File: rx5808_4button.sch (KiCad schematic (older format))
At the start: 53 parts, among them IC1 ATMEGA328-A, P1 CONN_01X02, P2 CONN_01X05, P3 CONN_02X03, P4 BNC, P5 BNC, P6 BNC, P7 CONN_01X02, SW1 SWITCH_INV, SW2 SW_PUSH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

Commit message: schaltplan weiter und mehr Footprints erstellt
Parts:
- removed D4, D5, D6, D7: weiß, LEDs:LED-0603, symbol LED
- removed R13, R14, R15, R16: 470, Resistors_SMD:R_0603, symbol R
- C5: value 22µ -> 10µ
- SW1: footprint (none) -> Apem:2543xN
- U2: footprint (none) -> Foxtech:RX5808
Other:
- note added: "Taster"
- note removed: "Taster mit Beleuchtung"
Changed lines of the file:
@@
 F 0 "U2" H 8400 2350 60  0000 C CNN
 F 1 "RX5808" H 8000 2350 60  0000 C CNN
-F 2 "" H 6750 2250 60  0001 C CNN
+F 2 "Foxtech:RX5808" H 6750 2250 60  0001 C CNN
 F 3 "" H 6750 2250 60  0000 C CNN
 	1    8200 3050
@@
 F 0 "SW1" H 8000 4450 50  0000 C CNN
 F 1 "SWITCH_INV" H 8050 4150 50  0000 C CNN
-F 2 "" H 8200 4300 60  0001 C CNN
+F 2 "Apem:2543xN" H 8200 4300 60  0001 C CNN
 F 3 "" H 8200 4300 60  0000 C CNN
 	1    8200 4300
@@
 P 3000 2900
 F 0 "C5" H 3050 3000 50  0000 L CNN
-F 1 "22µ" H 3050 2800 50  0000 L CNN
+F 1 "10µ" H 3050 2800 50  0000 L CNN
 F 2 "Capacitors_SMD:C_1206" H 3038 2750 30  0000 C CNN
 F 3 "" H 3000 2900 60  0000 C CNN
@@
 $EndComp
 $Comp
-L LED D4
-U 1 1 54EED267
-P 7600 6100
-F 0 "D4" H 7600 6200 50  0000 C CNN
-F 1 "weiß" H 7600 6000 50  0000 C CNN
-F 2 "LEDs:LED-0603" H 7600 6100 60  0001 C CNN
-F 3 "" H 7600 6100 60  0000 C CNN
-	1    7600 6100
-	0    1    1    0
-$EndComp
-$Comp
-L R R13
-U 1 1 54EED2CC
-P 7600 5650
-F 0 "R13" V 7680 5650 50  0000 C CNN
-F 1 "470" V 7607 5651 50  0000 C CNN
-F 2 "Resistors_SMD:R_0603" V 7530 5650 30  0001 C CNN
-F 3 "" H 7600 5650 30  0000 C CNN
-	1    7600 5650
-	1    0    0    -1
-$EndComp
-$Comp
-L GND #PWR050
-U 1 1 54EED36A
-P 7600 6300
-F 0 "#PWR050" H 7600 6050 60  0001 C CNN
-F 1 "GND" H 7600 6150 60  0000 C CNN
-F 2 "" H 7600 6300 60  0000 C CNN
-F 3 "" H 7600 6300 60  0000 C CNN
-	1    7600 6300
-	1    0    0    -1
-$EndComp
-$Comp
 L GND #PWR051
 U 1 1 54EED3A0
@@
 $EndComp
 $Comp
-L LED D5
-U 1 1 54EED5DC
-P 8200 6100
-F 0 "D5" H 8200 6200 50  0000 C CNN
-F 1 "weiß" H 8200 6000 50  0000 C CNN
-F 2 "LEDs:LED-0603" H 8200 6100 60  0001 C CNN
-F 3 "" H 8200 6100 60  0000 C CNN
-	1    8200 6100
-	0    1    1    0
-$EndComp
-$Comp
-L R R14
-U 1 1 54EED5E2
-P 8200 5650
-F 0 "R14" V 8280 5650 50  0000 C CNN
-F 1 "470" V 8207 5651 50  0000 C CNN
-F 2 "Resistors_SMD:R_0603" V 8130 5650 30  0001 C CNN
-F 3 "" H 8200 5650 30  0000 C CNN
-	1    8200 5650
-	1    0    0    -1
-$EndComp
-$Comp
-L GND #PWR052
-U 1 1 54EED5E8
-P 8200 6300
-F 0 "#PWR052" H 8200 6050 60  0001 C CNN
-F 1 "GND" H 8200 6150 60  0000 C CNN
-F 2 "" H 8200 6300 60  0000 C CNN
-F 3 "" H 8200 6300 60  0000 C CNN
-	1    8200 6300
-	1    0    0    -1
-$EndComp
-$Comp
 L GND #PWR053
 U 1 1 54EED5EE
@@
 $EndComp
 $Comp
-L LED D6
-U 1 1 54EED78E
-P 8800 6100
-F 0 "D6" H 8800 6200 50  0000 C CNN
-F 1 "weiß" H 8800 6000 50  0000 C CNN
-F 2 "LEDs:LED-0603" H 8800 6100 60  0001 C CNN
-F 3 "" H 8800 6100 60  0000 C CNN
-	1    8800 6100
-	0    1    1    0
-$EndComp
-$Comp
-L R R15
-U 1 1 54EED794
-P 8800 5650
-F 0 "R15" V 8880 5650 50  0000 C CNN
-F 1 "470" V 8807 5651 50  0000 C CNN
-F 2 "Resistors_SMD:R_0603" V 8730 5650 30  0001 C CNN
-F 3 "" H 8800 5650 30  0000 C CNN
-	1    8800 5650
-	1    0    0    -1
-$EndComp
-$Comp
-L GND #PWR054
-U 1 1 54EED79A
-P 8800 6300
-F 0 "#PWR054" H 8800 6050 60  0001 C CNN
-F 1 "GND" H 8800 6150 60  0000 C CNN
-F 2 "" H 8800 6300 60  0000 C CNN
-F 3 "" H 8800 6300 60  0000 C CNN
-	1    8800 6300
-	1    0    0    -1
-$EndComp
-$Comp
 L GND #PWR055
 U 1 1 54EED7A0
@@
 $EndComp
 $Comp
-L LED D7
-U 1 1 54EED7AC
-P 9400 6100
-F 0 "D7" H 9400 6200 50  0000 C CNN
-F 1 "weiß" H 9400 6000 50  0000 C CNN
-F 2 "LEDs:LED-0603" H 9400 6100 60  0001 C CNN
-F 3 "" H 9400 6100 60  0000 C CNN
-	1    9400 6100
-	0    1    1    0
-$EndComp
-$Comp
-L R R16
-U 1 1 54EED7B2
-P 9400 5650
-F 0 "R16" V 9480 5650 50  0000 C CNN
-F 1 "470" V 9407 5651 50  0000 C CNN
-F 2 "Resistors_SMD:R_0603" V 9330 5650 30  0001 C CNN
-F 3 "" H 9400 5650 30  0000 C CNN
-	1    9400 5650
-	1    0    0    -1
-$EndComp
-$Comp
-L GND #PWR056
-U 1 1 54EED7B8
-P 9400 6300
-F 0 "#PWR056" H 9400 6050 60  0001 C CNN
-F 1 "GND" H 9400 6150 60  0000 C CNN
-F 2 "" H 9400 6300 60  0000 C CNN
-F 3 "" H 9400 6300 60  0000 C CNN
-	1    9400 6300
-	1    0    0    -1
-$EndComp
-$Comp
 L GND #PWR057
 U 1 1 54EED7BE
@@
 Wire Wire Line
 	9100 5200 9100 5700
-$Comp
-L +5V #PWR059
-U 1 1 54EEE084
-P 7600 5400
-F 0 "#PWR059" H 7600 5250 60  0001 C CNN
-F 1 "+5V" H 7600 5540 60  0000 C CNN
-F 2 "" H 7600 5400 60  0000 C CNN
-F 3 "" H 7600 5400 60  0000 C CNN
-	1    7600 5400
-	1    0    0    -1
-$EndComp
-$Comp
-L +5V #PWR060
-U 1 1 54EEE12E
-P 8200 5400
-F 0 "#PWR060" H 8200 5250 60  0001 C CNN
-F 1 "+5V" H 8200 5540 60  0000 C CNN
-F 2 "" H 8200 5400 60  0000 C CNN
-F 3 "" H 8200 5400 60  0000 C CNN
-	1    8200 5400
-	1    0    0    -1
-$EndComp
-$Comp
-L +5V #PWR061
-U 1 1 54EEE16E
-P 8800 5400
-F 0 "#PWR061" H 8800 5250 60  0001 C CNN
-F 1 "+5V" H 8800 5540 60  0000 C CNN
-F 2 "" H 8800 5400 60  0000 C CNN
-F 3 "" H 8800 5400 60  0000 C CNN
-	1    8800 5400
-	1    0    0    -1
-$EndComp
-$Comp
-L +5V #PWR062
-U 1 1 54EEE1AE
-P 9400 5400
-F 0 "#PWR062" H 9400 5250 60  0001 C CNN
-F 1 "+5V" H 9400 5540 60  0000 C CNN
-F 2 "" H 9400 5400 60  0000 C CNN
-F 3 "" H 9400 5400 60  0000 C CNN
-	1    9400 5400
-	1    0    0    -1
-$EndComp
 Text Notes 9650 5900 0    60   ~ 0
-Taster mit Beleuchtung
+Taster
 $Comp
 L PWR_FLAG #FLG063

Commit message: Footprints für alle Taster und Schalter erstellt, inital commit für Platine
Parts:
- removed SW2, SW3, SW4, SW5: SW_PUSH, symbol SW_PUSH
- added R13, R14, R15, R16, R17, R18, R19, R20: 220, Resistors_SMD:R_0603, symbol R
- added U3, U4, U5, U6: RF15-Punktlicht, Rafi:RF15-Punktlicht, symbol RF15-Punktlicht
- L1: footprint (none) -> Inductors:self_cms_we-pd3
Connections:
- wire segments 79 -> 75
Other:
- note removed: "Taster"
- moved on the sheet: C1, C10, C11, C12, C2, C3, C4, C5, C6, C7, C8, C9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

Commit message: Layout fertig und Footprint für SMA geaddet.
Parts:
- removed P4: BNC, Pin_Headers:Pin_Header_Straight_1x02, symbol BNC
- added P10, P11, P8, P9: CONN_01X01, Mounting_Holes:MountingHole_3-5mm, symbol CONN_01X01
- added SMA_E1: SMA_EDGE, SMA_EDGE:SMA_EDGE, symbol SMA_EDGE
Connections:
- net GND: now also SMA_E1.0 (GND), SMA_E1.2 (GND)
- net at U2.2 (Ant): now also SMA_E1.1 (SIGNAL)
- no-connect marks 8 -> 12
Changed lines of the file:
@@
 EESchema Schematic File Version 2
+LIBS:SMA_EDGE
 LIBS:power
 LIBS:device
@@
 	0    -1   -1   0
 $EndComp
-$Comp
-L BNC P4
-U 1 1 54EE5D31
-P 9650 2400
-F 0 "P4" H 9660 2520 50  0000 C CNN
-F 1 "BNC" V 9760 2340 50  0000 C CNN
-F 2 "Pin_Headers:Pin_Header_Straight_1x02" H 9650 2400 60  0001 C CNN
-F 3 "" H 9650 2400 60  0000 C CNN
-	1    9650 2400
-	1    0    0    -1
-$EndComp
 Wire Wire Line
 	9500 2400 8900 2400
@@
 L GND #PWR026
 U 1 1 54EE5DF8
-P 9650 2600
-F 0 "#PWR026" H 9650 2350 60  0001 C CNN
-F 1 "GND" H 9650 2450 60  0000 C CNN
-F 2 "" H 9650 2600 60  0000 C CNN
-F 3 "" H 9650 2600 60  0000 C CNN
-	1    9650 2600
-	1    0    0    -1
+P 9500 2500
+F 0 "#PWR026" H 9500 2250 60  0001 C CNN
+F 1 "GND" H 9500 2350 60  0000 C CNN
+F 2 "" H 9500 2500 60  0000 C CNN
+F 3 "" H 9500 2500 60  0000 C CNN
+	1    9500 2500
+	0    1    1    0
 $EndComp
 Text Label 7200 2500 0    60   ~ 0
@@
 Text Notes 9900 4500 0    60   ~ 0
 mini Monitor
-Text Notes 9900 2400 0    60   ~ 0
+Text Notes 9850 2700 0    60   ~ 0
 5,8GHz Antenne
 $Comp
@@
 	1    0    0    -1
 $EndComp
-$Comp
-L CONN_01X02 P7
-U 1 1 54EEC3F3
-P 9700 1450
-F 0 "P7" H 9700 1600 50  0000 C CNN
-F 1 "CONN_01X02" V 9800 1450 50  0000 C CNN
-F 2 "Pin_Headers:Pin_Header_Straight_1x02" H 9700 1450 60  0001 C CNN
-F 3 "" H 9700 1450 60  0000 C CNN
-	1    9700 1450
-	1    0    0    -1
-$EndComp
 Text Notes 9600 1100 0    60   ~ 0
 Audio\nOut
@@
 	1    0    0    -1
 $EndComp
+$Comp
+L CONN_01X01 P8
+U 1 1 54F07FE7
+P 2550 7450
+F 0 "P8" H 2550 7550 50  0000 C CNN
+F 1 "CONN_01X01" V 2650 7450 50  0000 C CNN
+F 2 "Mounting_Holes:MountingHole_3-5mm" H 2550 7450 60  0001 C CNN
+F 3 "" H 2550 7450 60  0000 C CNN
+	1    2550 7450
+	0    1    1    0
+$EndComp
+NoConn ~ 2550 7250
+$Comp
+L CONN_01X01 P9
+U 1 1 54F082A0
+P 2950 7450
+F 0 "P9" H 2950 7550 50  0000 C CNN
+F 1 "CONN_01X01" V 3050 7450 50  0000 C CNN
+F 2 "Mounting_Holes:MountingHole_3-5mm" H 2950 7450 60  0001 C CNN
+F 3 "" H 2950 7450 60  0000 C CNN
+	1    2950 7450
+	0    1    1    0
+$EndComp
+NoConn ~ 2950 7250
+$Comp
+L CONN_01X01 P10
+U 1 1 54F08359
+P 3300 7450
+F 0 "P10" H 3300 7550 50  0000 C CNN
+F 1 "CONN_01X01" V 3400 7450 50  0000 C CNN
+F 2 "Mounting_Holes:MountingHole_3-5mm" H 3300 7450 60  0001 C CNN
+F 3 "" H 3300 7450 60  0000 C CNN
+	1    3300 7450
+	0    1    1    0
+$EndComp
+NoConn ~ 3300 7250
+$Comp
+L CONN_01X01 P11
+U 1 1 54F08360
+P 3700 7450
+F 0 "P11" H 3700 7550 50  0000 C CNN
+F 1 "CONN_01X01" V 3800 7450 50  0000 C CNN
+F 2 "Mounting_Holes:MountingHole_3-5mm" H 3700 7450 60  0001 C CNN
+F 3 "" H 3700 7450 60  0000 C CNN
+	1    3700 7450
+	0    1    1    0
+$EndComp
+NoConn ~ 3700 7250
+$Comp
+L CONN_01X02 P7
+U 1 1 54EEC3F3
+P 9700 1450
+F 0 "P7" H 9700 1600 50  0000 C CNN
+F 1 "CONN_01X02" V 9800 1450 50  0000 C CNN
+F 2 "Pin_Headers:Pin_Header_Straight_1x02" H 9700 1450 60  0001 C CNN
+F 3 "" H 9700 1450 60  0000 C CNN
+	1    9700 1450
+	1    0    0    -1
+$EndComp
+$Comp
+L SMA_EDGE SMA_E1
+U 1 1 54F0E594
+P 9850 2400
+F 0 "SMA_E1" H 10000 2700 60  0000 C CNN
+F 1 "SMA_EDGE" H 10000 2600 60  0000 C CNN
+F 2 "SMA_EDGE:SMA_EDGE" H 9850 2400 60  0001 C CNN
+F 3 "" H 9850 2400 60  0000 C CNN
+	1    9850 2400
+	1    0    0    -1
+$EndComp
+$Comp
+L GND #PWR075
+U 1 1 54F0E7D0
+P 9500 2300
+F 0 "#PWR075" H 9500 2050 60  0001 C CNN
+F 1 "GND" H 9500 2150 60  0000 C CNN
+F 2 "" H 9500 2300 60  0000 C CNN
+F 3 "" H 9500 2300 60  0000 C CNN
+	1    9500 2300
+	0    1    1    0
+$EndComp
 $EndSCHEMATC

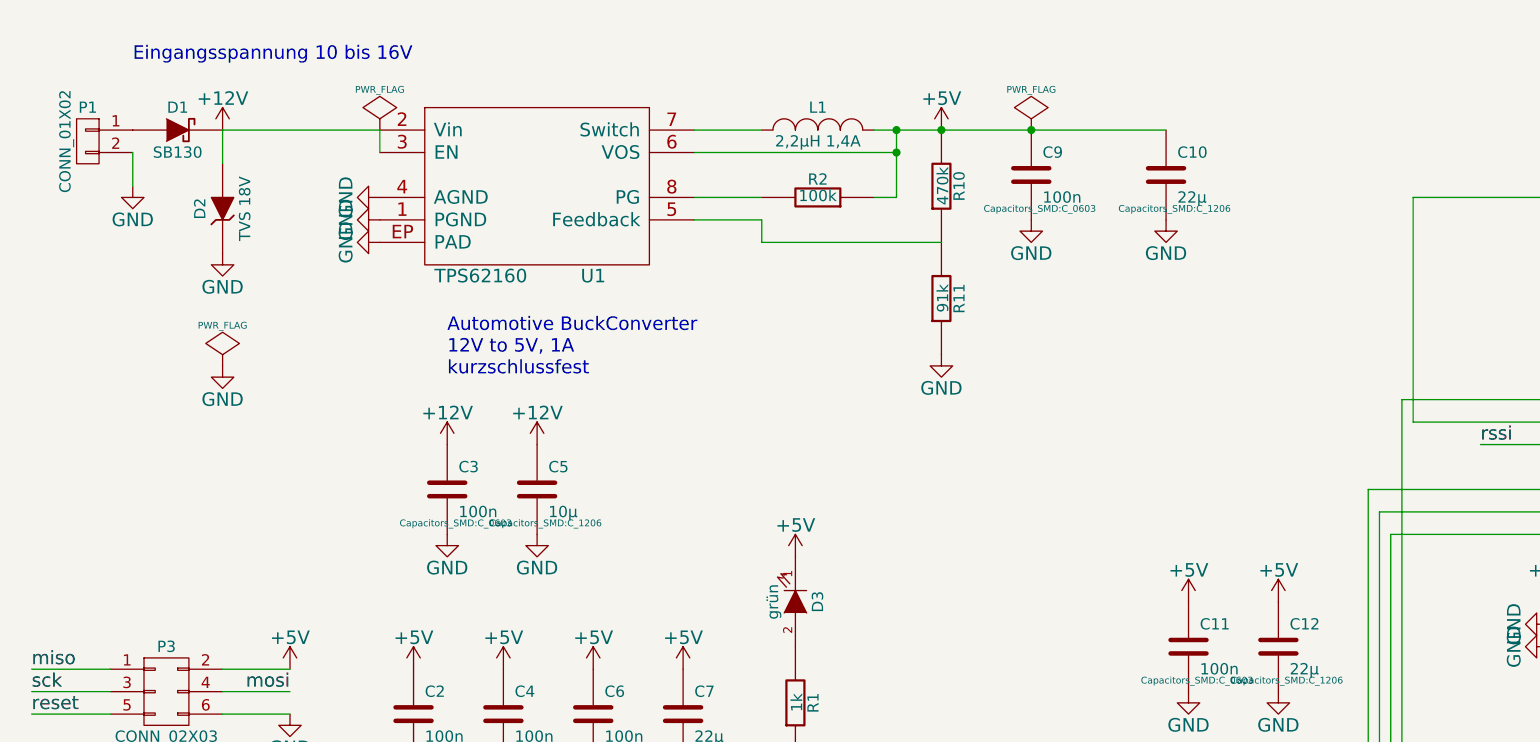
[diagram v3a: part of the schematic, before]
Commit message: andere Spule und neues Layout für den Schaltwandler
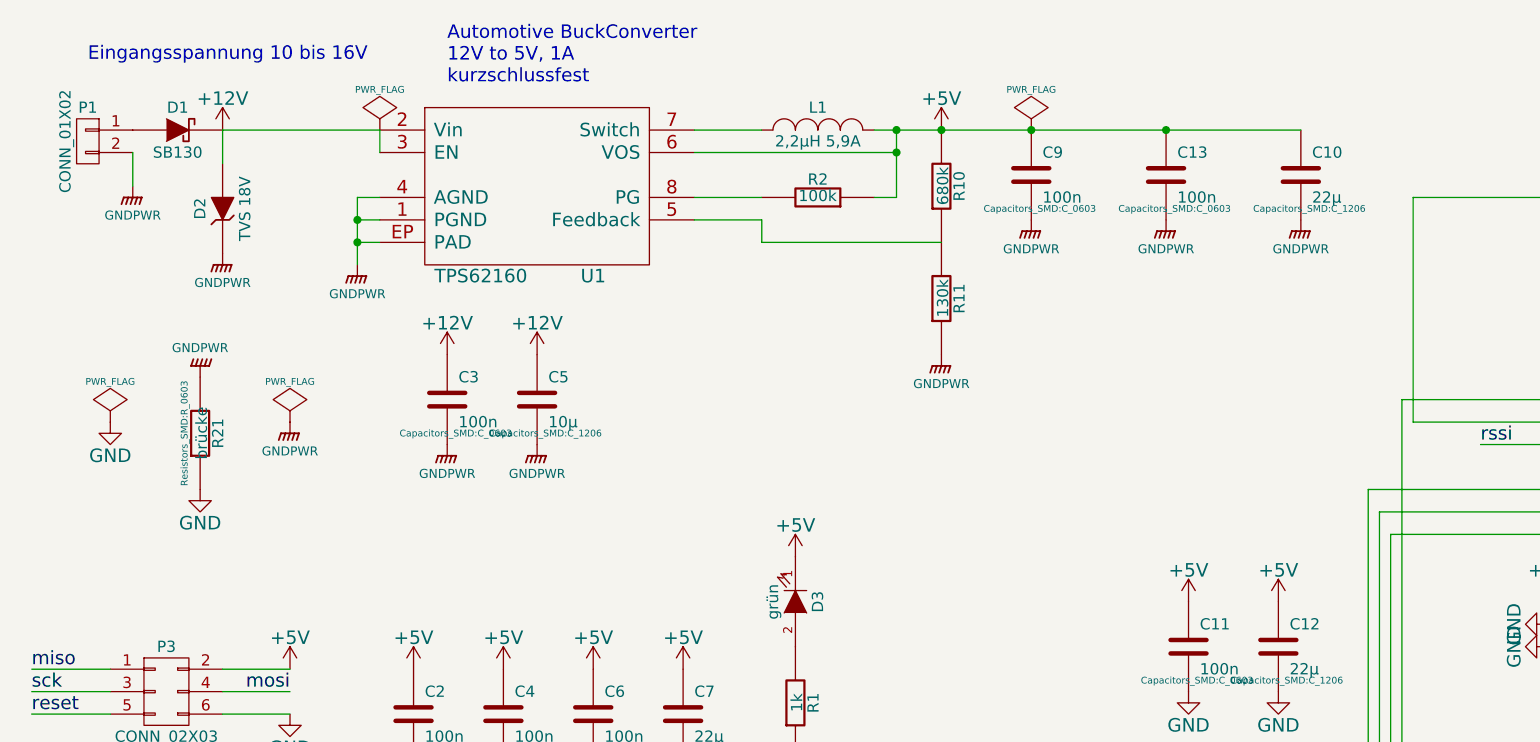
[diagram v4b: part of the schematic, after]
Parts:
- added C13: 100n, Capacitors_SMD:C_0603, symbol C
- added R21: brücke, Resistors_SMD:R_0603, symbol R
- L1: value 2,2µH 1,4A -> 2,2µH 5,9A; footprint Inductors:self_cms_we-pd3 -> TDK_Inductor:VLF4012A; Name (none) -> VLF4012S-3R3
- R10: value 470k -> 680k
- R11: value 91k -> 130k
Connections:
- net +5V: now also C13.1
- net GND: now also R21.2; no longer C10.2, C3.2, C5.2, C9.2, D2.1 (K), P1.2 (P2), R11.2, U1.1 (PGND), U1.4 (AGND), U1.EP (PAD)
- new net GNDPWR: C10.2, C13.2, C3.2, C5.2, C9.2, D2.1 (K), P1.2 (P2), R11.2, R21.1, U1.1 (PGND), U1.4 (AGND), U1.EP (PAD)
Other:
- moved on the sheet: C10, C3, C5

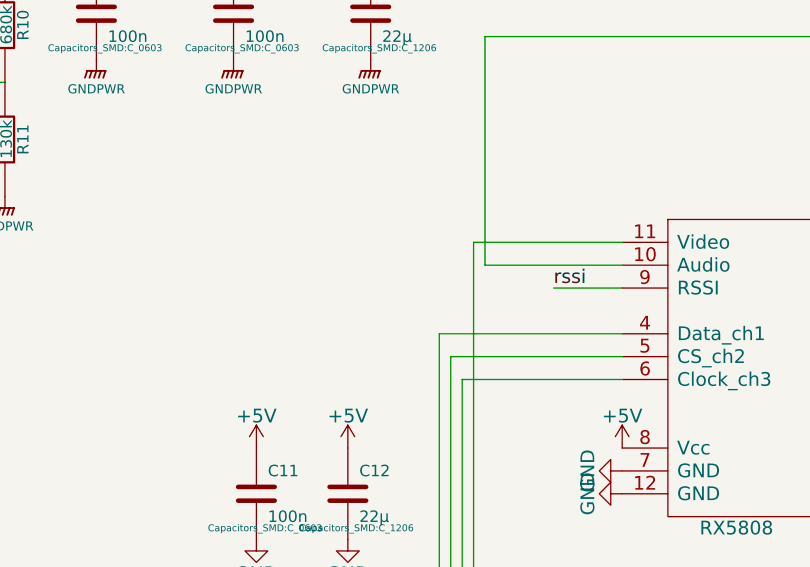
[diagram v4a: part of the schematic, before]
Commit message: rssi-anschluss für externe RSSI-Anzeige dazugebaut
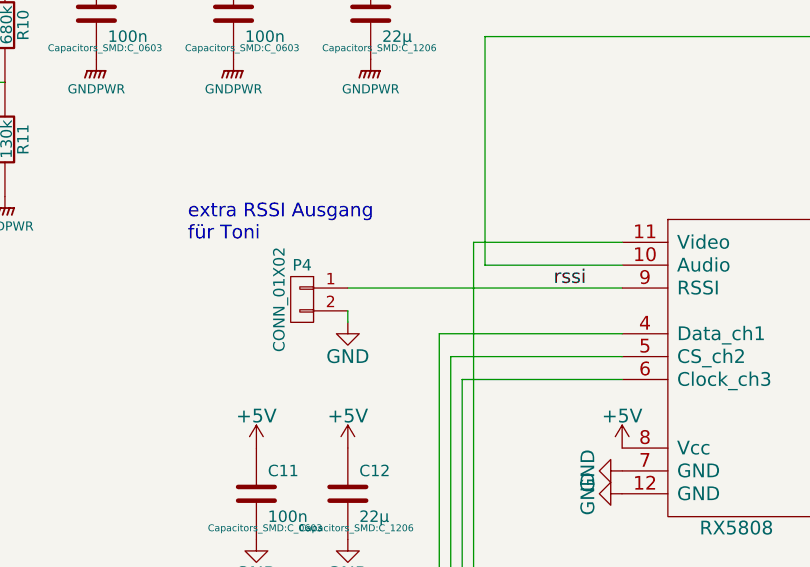
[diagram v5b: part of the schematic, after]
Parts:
- added P4: CONN_01X02, Pin_Headers:Pin_Header_Straight_1x02, symbol CONN_01X02
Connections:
- net GND: now also P4.2 (P2)
- net rssi: now also P4.1 (P1)
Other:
- note added: "extra RSSI Ausgang\nfür Toni"
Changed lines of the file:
@@
 rssi
 Wire Wire Line
-	7200 2500 7500 2500
+	6300 2500 7500 2500
 $Comp
 L BNC P5
@@
 	1    0    0    -1
 $EndComp
+$Comp
+L CONN_01X02 P4
+U 1 1 54F268DC
+P 6100 2550
+F 0 "P4" H 6100 2700 50  0000 C CNN
+F 1 "CONN_01X02" V 6200 2550 50  0000 C CNN
+F 2 "Pin_Headers:Pin_Header_Straight_1x02" H 6100 2550 60  0001 C CNN
+F 3 "" H 6100 2550 60  0000 C CNN
+	1    6100 2550
+	-1   0    0    -1
+$EndComp
+$Comp
+L GND #PWR079
+U 1 1 54F26955
+P 6300 2650
+F 0 "#PWR079" H 6300 2400 60  0001 C CNN
+F 1 "GND" H 6300 2500 60  0000 C CNN
+F 2 "" H 6300 2650 60  0000 C CNN
+F 3 "" H 6300 2650 60  0000 C CNN
+	1    6300 2650
+	1    0    0    -1
+$EndComp
+Wire Wire Line
+	6300 2650 6300 2600
+Text Notes 5600 2300 0    60   ~ 0
+extra RSSI Ausgang\nfür Toni
 $EndSCHEMATC

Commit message: Layout fertig - cinchbuchsen für Video eingebaut.
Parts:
- P1: footprint Pin_Headers:Pin_Header_Straight_1x02 -> Sockets_MOLEX_KK-System:Socket_MOLEX-KK-RM2-54mm_Lock_2pin_straight
- P5, P6: footprint Pin_Headers:Pin_Header_Straight_1x02 -> RCA:Cinch_angled_mono
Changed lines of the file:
@@
 LIBS:Rafi
 LIBS:rx5808_4button-cache
-EELAYER 24 0
+EELAYER 25 0
 EELAYER END
 $Descr A4 11693 8268
@@
 F 0 "P5" H 9660 3920 50  0000 C CNN
 F 1 "BNC" V 9760 3740 50  0000 C CNN
-F 2 "Pin_Headers:Pin_Header_Straight_1x02" H 9650 3800 60  0001 C CNN
+F 2 "RCA:Cinch_angled_mono" H 9650 3800 60  0001 C CNN
 F 3 "" H 9650 3800 60  0000 C CNN
 	1    9650 3800
@@
 F 0 "P6" H 9660 4620 50  0000 C CNN
 F 1 "BNC" V 9760 4440 50  0000 C CNN
-F 2 "Pin_Headers:Pin_Header_Straight_1x02" H 9650 4500 60  0001 C CNN
+F 2 "RCA:Cinch_angled_mono" H 9650 4500 60  0001 C CNN
 F 3 "" H 9650 4500 60  0000 C CNN
 	1    9650 4500
@@
 F 0 "P1" H 1000 1300 50  0000 C CNN
 F 1 "CONN_01X02" V 1100 1150 50  0000 C CNN
-F 2 "Pin_Headers:Pin_Header_Straight_1x02" H 1000 1150 60  0001 C CNN
+F 2 "Sockets_MOLEX_KK-System:Socket_MOLEX-KK-RM2-54mm_Lock_2pin_straight" H 1000 1150 60  0001 C CNN
 F 3 "" H 1000 1150 60  0000 C CNN
 	1    1000 1150

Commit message: 130k-Ohm durch zwei parallele Widerstände ersetzt, um eine vollständige E12-Kompatibilität gewährleisten zu können
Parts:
- added R22: 150k, Resistors_SMD:R_0603, symbol R
- R11: value 130k -> 1M; footprint Resistors_SMD:R_0805 -> Resistors_SMD:R_0603
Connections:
- net GNDPWR: now also R22.2
- net at R10.2, R11.1, U1.5 (Feedback): now also R22.1
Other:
- note added: "Eingangsspannung 8 bis 16V"
- note removed: "Eingangsspannung 10 bis 16V"
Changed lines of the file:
@@
 P 4800 1850
 F 0 "R11" V 4880 1850 50  0000 C CNN
-F 1 "130k" V 4807 1851 50  0000 C CNN
-F 2 "Resistors_SMD:R_0805" V 4730 1850 30  0001 C CNN
+F 1 "1M" V 4807 1851 50  0000 C CNN
+F 2 "Resistors_SMD:R_0603" V 4730 1850 30  0001 C CNN
 F 3 "" H 4800 1850 30  0000 C CNN
 	1    4800 1850
@@
 $EndComp
 Wire Wire Line
-	4800 1600 4000 1600
+	4000 1600 4950 1600
 Wire Wire Line
 	4000 1600 4000 1500
@@
 $EndComp
 Text Notes 1000 800  0    60   ~ 0
-Eingangsspannung 10 bis 16V
+Eingangsspannung 8 bis 16V
 Text Notes 2600 900  0    60   ~ 0
 Automotive BuckConverter\n12V to 5V, 1A\nkurzschlussfest
@@
 Text Notes 5600 2300 0    60   ~ 0
 extra RSSI Ausgang\nfür Toni
+$Comp
+L R R22
+U 1 1 551FF942
+P 4950 1850
+F 0 "R22" V 5030 1850 50  0000 C CNN
+F 1 "150k" V 4957 1851 50  0000 C CNN
+F 2 "Resistors_SMD:R_0603" V 4880 1850 30  0001 C CNN
+F 3 "" H 4950 1850 30  0000 C CNN
+	1    4950 1850
+	1    0    0    -1
+$EndComp
+$Comp
+L GNDPWR #PWR080
+U 1 1 551FFB48
+P 4950 2100
+F 0 "#PWR080" H 4950 1900 40  0001 C CNN
+F 1 "GNDPWR" H 4950 1970 40  0000 C CNN
+F 2 "" H 4950 2050 60  0000 C CNN
+F 3 "" H 4950 2050 60  0000 C CNN
+	1    4950 2100
+	1    0    0    -1
+$EndComp
+Connection ~ 4800 1600
 $EndSCHEMATC
